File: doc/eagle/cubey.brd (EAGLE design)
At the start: 95.5 x 61.1 mm, 25 parts, among them K1 PIN20X2

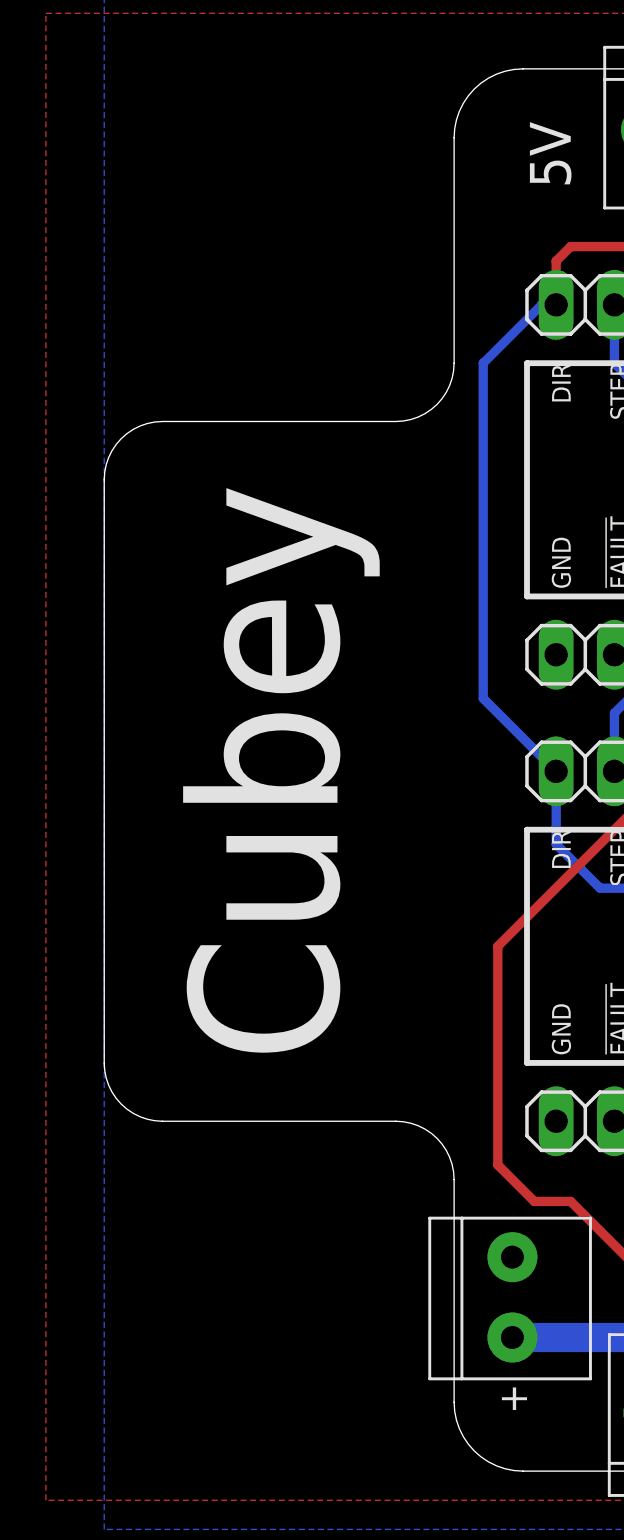
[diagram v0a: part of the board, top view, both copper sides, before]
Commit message: remove the "tongue" from the board layout. SVG logo.
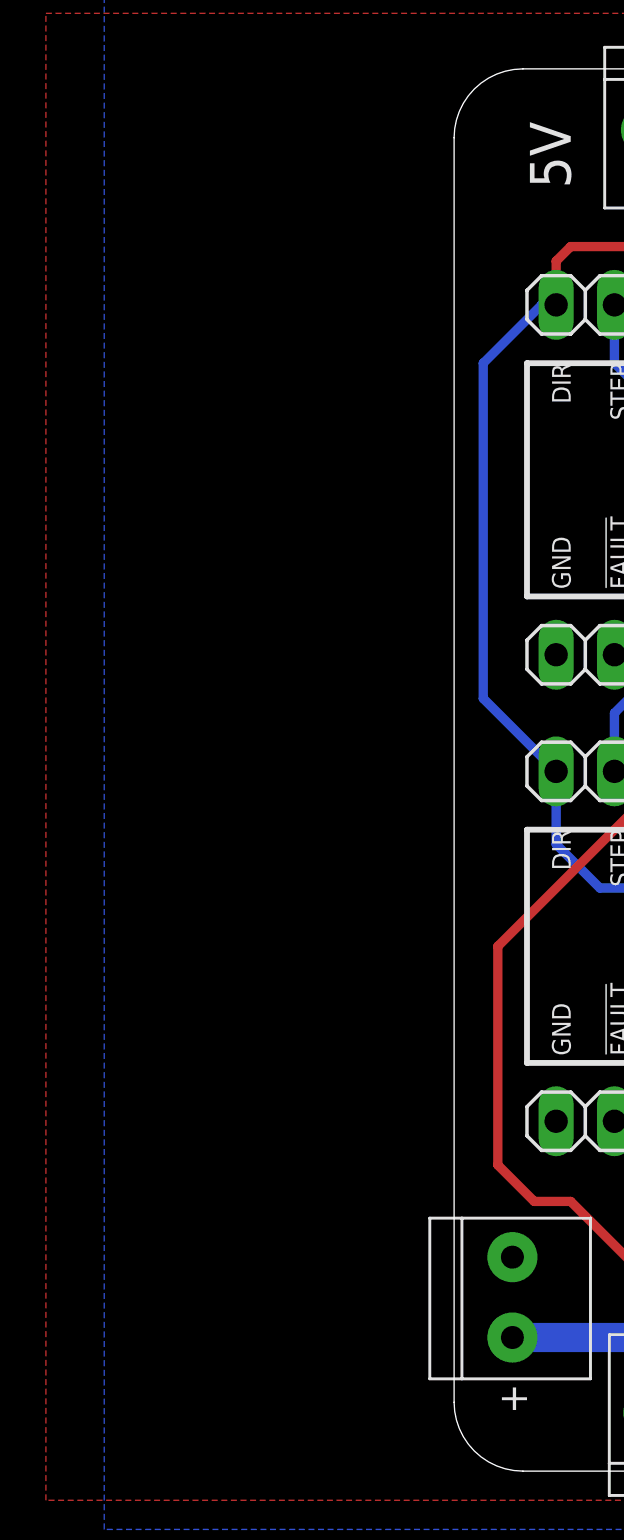
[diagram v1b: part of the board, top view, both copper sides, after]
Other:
- board size 95.5 x 61.1 mm -> 80.2 x 61.1 mm
- board text removed: "Cubey"
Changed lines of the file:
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@@
 <wire x1="77.24" y1="61.08" x2="3" y2="61.08" width="0" layer="20"/>
 <wire x1="3" y1="61.08" x2="0" y2="58.08" width="0" layer="20" curve="90"/>
-<wire x1="0" y1="58.08" x2="0" y2="48.26" width="0" layer="20"/>
-<wire x1="0" y1="48.26" x2="-2.54" y2="45.72" width="0" layer="20" curve="-90"/>
-<wire x1="-2.54" y1="45.72" x2="-12.7" y2="45.72" width="0" layer="20"/>
-<wire x1="-12.7" y1="45.72" x2="-15.24" y2="43.18" width="0" layer="20" curve="90"/>
-<wire x1="-15.24" y1="43.18" x2="-15.24" y2="17.78" width="0" layer="20"/>
-<wire x1="-15.24" y1="17.78" x2="-12.7" y2="15.24" width="0" layer="20" curve="90"/>
-<wire x1="-12.7" y1="15.24" x2="-2.54" y2="15.24" width="0" layer="20"/>
-<wire x1="-2.54" y1="15.24" x2="0" y2="12.7" width="0" layer="20" curve="-90"/>
-<wire x1="0" y1="12.7" x2="0" y2="3" width="0" layer="20"/>
+<wire x1="0" y1="58.08" x2="0" y2="3" width="0" layer="20"/>
 <hole x="18.74" y="8.58" drill="2.8"/>
 <hole x="18.74" y="57.58" drill="2.8"/>
@@
 <text x="71.12" y="38.4175" size="0.8128" layer="25" font="vector" rot="R90">GND</text>
 <text x="73.66" y="38.4175" size="0.8128" layer="25" font="vector" rot="R90">VMOT</text>
-<text x="-5.08" y="17.78" size="6.4516" layer="25" rot="R90">Cubey</text>
 </plain>
 <attributes>

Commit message: Added Solder jumpers for M0, M1 and M2
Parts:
- added SJ1, SJ2, SJ3: (no value), jumper:SJ
- moved 5V_PWR 2.54 mm to (12.7, 58.4)
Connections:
- new net MODE0: JP1.2, JP11.2, JP3.2, JP5.2, JP7.2, JP9.2, SJ1.2
- new net MODE1: JP1.3, JP11.3, JP3.3, JP5.3, JP7.3, JP9.3, SJ2.2
- new net MODE2: JP1.4, JP11.4, JP3.4, JP5.4, JP7.4, JP9.4, SJ3.2
- net +5V: now also SJ1.1, SJ2.1, SJ3.1
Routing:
- net MODE2: track 0.00 -> 136.5 mm, vias 0 -> 2
- net MODE1: track 0.00 -> 135.4 mm, vias 0 -> 3
- net MODE0: track 0.00 -> 126.5 mm, vias 0 -> 3
- net B2(4): track 68.9 -> 44.4 mm
- net DIR: track 147.3 -> 124.4 mm
- net A2(4): track 56.3 -> 33.6 mm
- net B1(4): track 61.4 -> 39.9 mm, vias 1 -> 0
- net A2(6): track 67.4 -> 46.5 mm
- net A1(5): track 46.3 -> 28.4 mm, vias 2 -> 0
- net B2(6): track 59.1 -> 42.3 mm
- net B1(6): track 60.5 -> 43.9 mm, vias 1 -> 0
- net VCC: track 183.8 -> 171.6 mm
- net A2(5): track 43.8 -> 33.0 mm
- net B2(5): track 53.3 -> 43.5 mm, vias 3 -> 1
- net A1(6): track 42.0 -> 51.8 mm
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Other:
- board text added: "MODE 0"
- board text added: "MODE 1"
- board text added: "MODE 2"

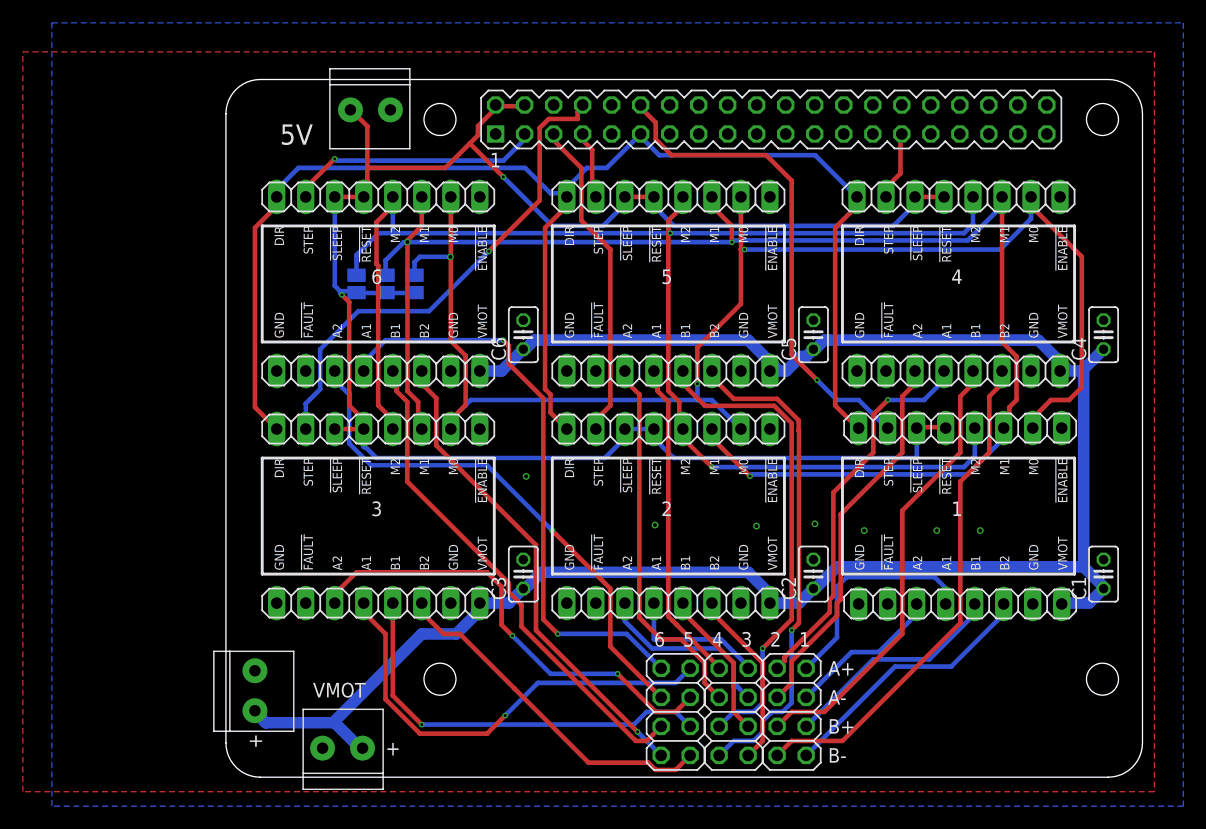
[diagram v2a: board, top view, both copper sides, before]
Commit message: Rename signals in Cubey PCB design. Finalized V2 with ENABLE pin.
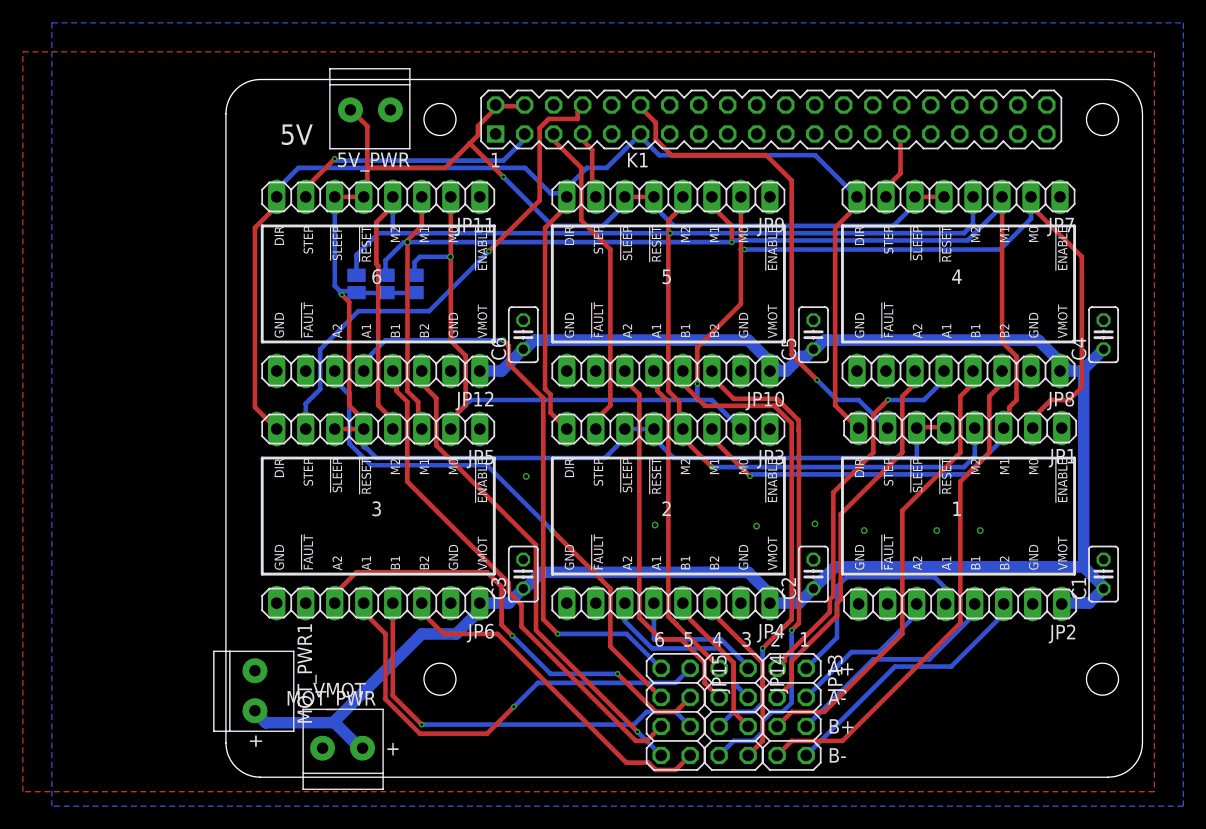
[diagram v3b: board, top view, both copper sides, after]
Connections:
- net A1(1) renamed A1_UP
- net A1(2) renamed A1_RIGHT
- net A1(3) renamed A1_FRONT
- net A1(4) renamed A1_DOWN
- net A1(5) renamed A1_LEFT
- net A1(6) renamed A1_BACK
- net A2(1) renamed A2_UP
- net A2(2) renamed A2_RIGHT
- net A2(3) renamed A2_FRONT
- net A2(4) renamed A2_DOWN
- net A2(5) renamed A2_LEFT
- net A2(6) renamed A2_BACK
- net B1(1) renamed B1_UP
- net B1(2) renamed B1_RIGHT
- net B1(3) renamed B1_FRONT
- net B1(4) renamed B1_DOWN
- net B1(5) renamed B1_LEFT
- net B1(6) renamed B1_BACK
- net B2(1) renamed B2_UP
- net B2(2) renamed B2_RIGHT
- net B2(3) renamed B2_FRONT
- net B2(4) renamed B2_DOWN
- net B2(5) renamed B2_LEFT
- net B2(6) renamed B2_BACK
- net STEP(1) renamed STEP_UP
- net STEP(2) renamed STEP_RIGHT
- net STEP(3) renamed STEP_FRONT
- net STEP(4) renamed STEP_DOWN
- net STEP(5) renamed STEP_LEFT
- net STEP(6) renamed STEP_BACK
